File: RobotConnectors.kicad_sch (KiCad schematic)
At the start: 67 parts, among them J1 Conn_02x11_Top_Bottom, J10 Conn_01x05, J11 Conn_01x03_Male, J12 Conn_01x03_Male, J13 Conn_01x03_Male, J14 Conn_01x03_Male, J17 Conn_01x02, J18 Conn_01x02, J19 Conn_01x04, J2 Conn_02x04_Top_Bottom, J21 Conn_01x05, J27 Conn_01x03_Male, J28 Conn_01x03_Male, J29 Conn_01x03_Male, J3 Conn_01x02, J30 Conn_01x03_Male, J4 Conn_01x04, J5 Conn_01x04, J6 Conn_01x04, J7 Conn_01x04, J8 Conn_01x04, J9 Conn_01x04, U11 TXS0108EPW, U12 TXS0108EPW, U14 Fuse Holder, U15 Fuse Holder, U16 Fuse Holder, U17 Fuse Holder, U2 TPS2065CDBV, U28 Fuse 2A, U29 Fuse 2A

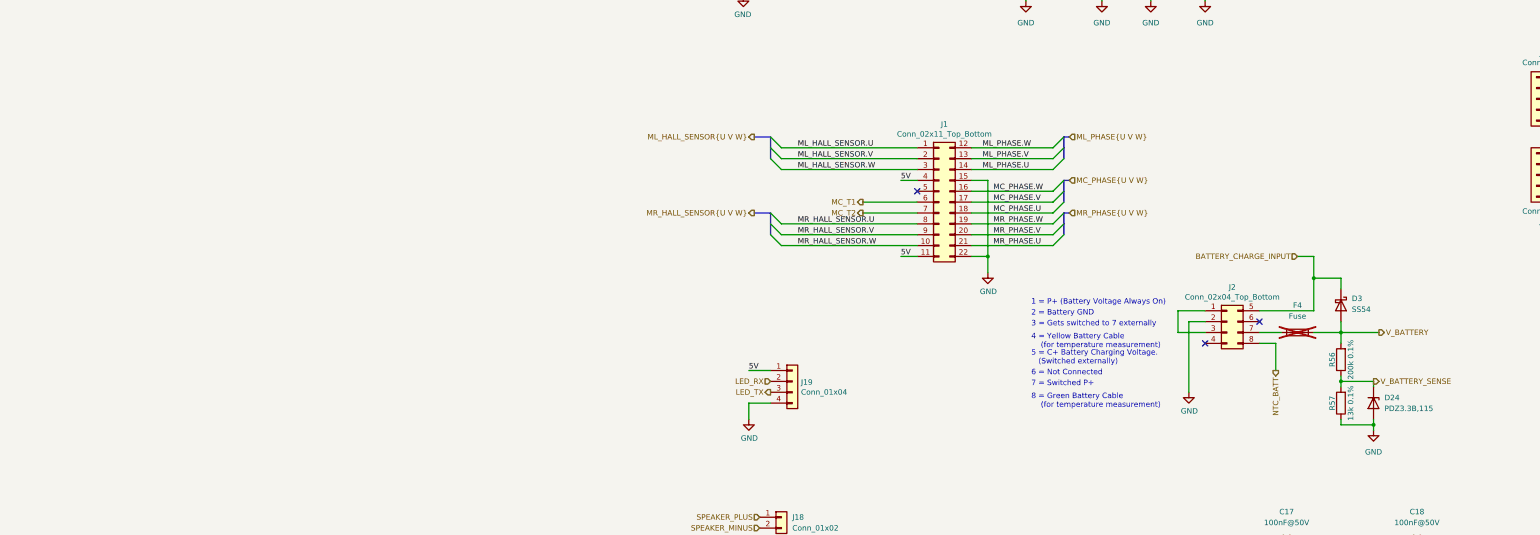
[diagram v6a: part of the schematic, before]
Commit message: Fix V_BATT ADC
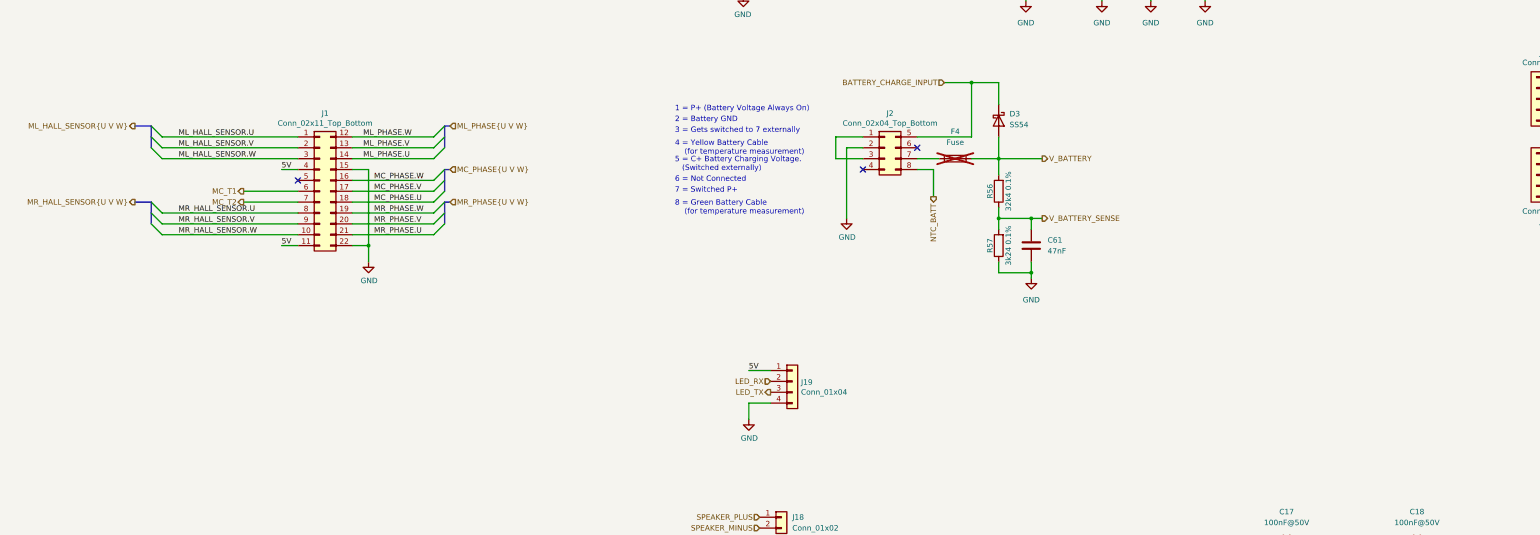
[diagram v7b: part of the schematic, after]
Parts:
- removed D24: PDZ3.3B,115, Diode_SMD:D_SOD-323, symbol Device:D_Zener
- added C61: 47nF, Capacitor_SMD:C_0603_1608Metric, symbol Device:C
- R56: value 200k 0.1% -> 32k4 0.1%; footprint Resistor_SMD:R_0402_1005Metric -> Resistor_SMD:R_0603_1608Metric; JLC C728556 -> C861323
- R57: value 13k 0.1% -> 3k24 0.1%; footprint Resistor_SMD:R_0402_1005Metric -> Resistor_SMD:R_0603_1608Metric; JLC C852524 -> C728589
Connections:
- net GND: now also C61.2
- net V_BATTERY_SENSE: now also C61.1
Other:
- moved on the sheet: D3, F4, J1, J2, R56, R57

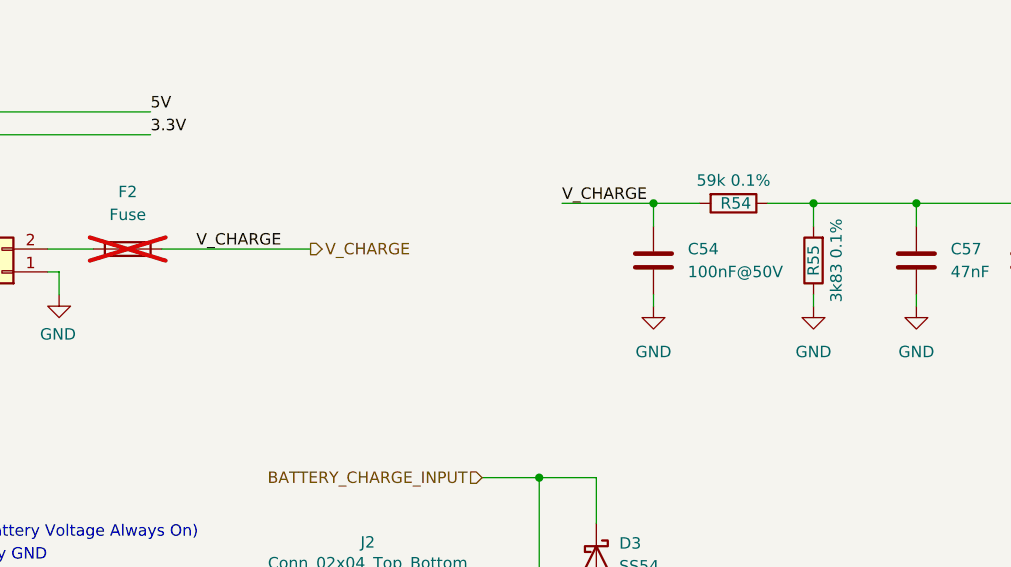
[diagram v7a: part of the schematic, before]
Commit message: V_CHARGE TVS protection and V_CHARGE ADC divider adjustment
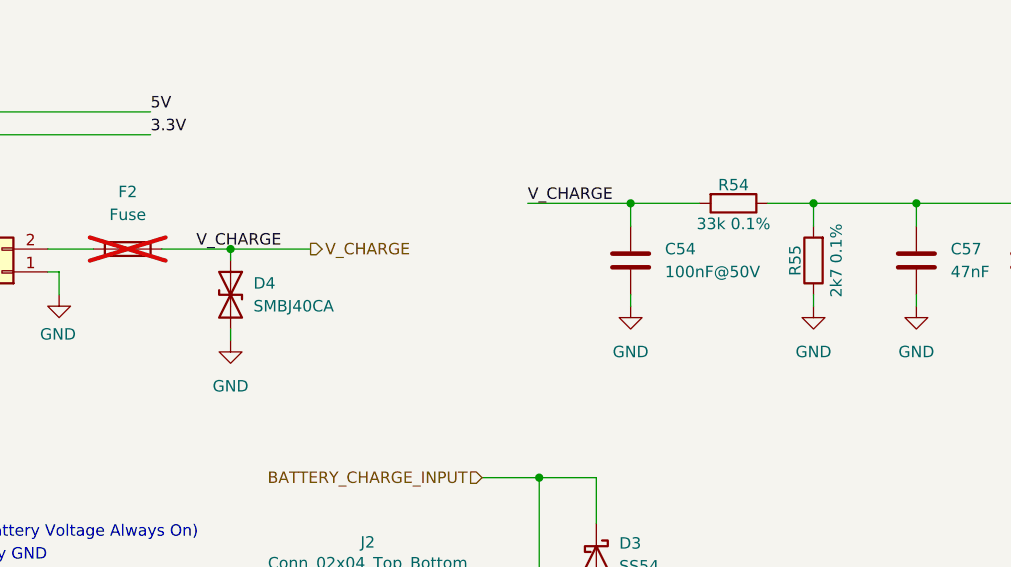
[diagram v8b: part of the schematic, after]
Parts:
- added D4: SMBJ40CA, Diode_SMD:D_SMB, symbol Device:D_TVS
- R54: value 59k 0.1% -> 33k 0.1%; JLC C852853 -> C5455470
- R55: value 3k83 0.1% -> 2k7 0.1%; JLC C852772 -> C852706
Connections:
- net GND: now also D4.2 (A2)
- net V_CHARGE: now also D4.1 (A1)
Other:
- moved on the sheet: C54
